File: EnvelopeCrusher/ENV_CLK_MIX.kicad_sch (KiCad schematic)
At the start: 15 parts, among them U6 TL072

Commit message: Completed Schematic
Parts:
- gave numbers to parts that had none: 13
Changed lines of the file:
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@@
   (symbol (lib_id "Device:R") (at 119.38 86.36 90) (mirror x) (unit 1)
     (in_bom yes) (on_board yes)
-    (property "Reference" "R?" (id 0) (at 119.38 83.82 90))
+    (property "Reference" "R26" (id 0) (at 119.38 83.82 90))
     (property "Value" "10K" (id 1) (at 119.38 88.9 90))
     (property "Footprint" "Resistor_SMD:R_0805_2012Metric_Pad1.20x1.40mm_HandSolder" (id 2) (at 119.38 84.582 90)
@@
   (symbol (lib_id "power:+5V") (at 44.45 133.9779 0) (unit 1)
     (in_bom yes) (on_board yes) (fields_autoplaced)
-    (property "Reference" "#PWR?" (id 0) (at 44.45 137.7879 0)
+    (property "Reference" "#PWR069" (id 0) (at 44.45 137.7879 0)
       (effects (font (size 1.27 1.27)) hide)
     )
@@
   (symbol (lib_id "Jumper:SolderJumper_2_Bridged") (at 101.6 58.42 0) (unit 1)
     (in_bom yes) (on_board yes)
-    (property "Reference" "JP?" (id 0) (at 101.6 55.88 0))
+    (property "Reference" "JP8" (id 0) (at 101.6 55.88 0))
     (property "Value" "SolderJumper_2_Bridged" (id 1) (at 101.6 54.61 0)
       (effects (font (size 1.27 1.27)) hide)
@@
   (symbol (lib_id "power:GND") (at 138.43 106.68 0) (unit 1)
     (in_bom yes) (on_board yes) (fields_autoplaced)
-    (property "Reference" "#PWR?" (id 0) (at 138.43 113.03 0)
+    (property "Reference" "#PWR073" (id 0) (at 138.43 113.03 0)
       (effects (font (size 1.27 1.27)) hide)
     )
@@
   (symbol (lib_id "Device:R") (at 119.38 95.25 90) (mirror x) (unit 1)
     (in_bom yes) (on_board yes)
-    (property "Reference" "R?" (id 0) (at 119.38 92.71 90))
+    (property "Reference" "R27" (id 0) (at 119.38 92.71 90))
     (property "Value" "10K" (id 1) (at 119.38 97.79 90))
     (property "Footprint" "Resistor_SMD:R_0805_2012Metric_Pad1.20x1.40mm_HandSolder" (id 2) (at 119.38 93.472 90)
@@
   (symbol (lib_id "Jumper:SolderJumper_2_Bridged") (at 101.6 95.25 0) (unit 1)
     (in_bom yes) (on_board yes)
-    (property "Reference" "JP?" (id 0) (at 101.6 92.71 0))
+    (property "Reference" "JP10" (id 0) (at 101.6 92.71 0))
     (property "Value" "SolderJumper_2_Bridged" (id 1) (at 101.6 91.44 0)
       (effects (font (size 1.27 1.27)) hide)
@@
   (symbol (lib_id "Device:C") (at 120.65 149.86 180) (unit 1)
     (in_bom yes) (on_board yes)
-    (property "Reference" "C?" (id 0) (at 121.92 147.32 0)
+    (property "Reference" "C50" (id 0) (at 121.92 147.32 0)
       (effects (font (size 1.27 1.27)) (justify right))
     )
@@
   (symbol (lib_id "power:GND") (at 31.75 160.02 0) (unit 1)
     (in_bom yes) (on_board yes) (fields_autoplaced)
-    (property "Reference" "#PWR?" (id 0) (at 31.75 166.37 0)
+    (property "Reference" "#PWR068" (id 0) (at 31.75 166.37 0)
       (effects (font (size 1.27 1.27)) hide)
     )
@@
   (symbol (lib_id "power:-5V") (at 107.95 133.9779 0) (unit 1)
     (in_bom yes) (on_board yes) (fields_autoplaced)
-    (property "Reference" "#PWR?" (id 0) (at 107.95 131.4379 0)
+    (property "Reference" "#PWR070" (id 0) (at 107.95 131.4379 0)
       (effects (font (size 1.27 1.27)) hide)
     )
@@
   (symbol (lib_id "Jumper:SolderJumper_2_Bridged") (at 101.6 86.36 0) (unit 1)
     (in_bom yes) (on_board yes)
-    (property "Reference" "JP?" (id 0) (at 101.6 83.82 0))
+    (property "Reference" "JP9" (id 0) (at 101.6 83.82 0))
     (property "Value" "SolderJumper_2_Bridged" (id 1) (at 101.6 82.55 0)
       (effects (font (size 1.27 1.27)) hide)
@@
   (symbol (lib_id "Device:R") (at 119.38 49.53 90) (mirror x) (unit 1)
     (in_bom yes) (on_board yes)
-    (property "Reference" "R?" (id 0) (at 119.38 46.99 90))
+    (property "Reference" "R24" (id 0) (at 119.38 46.99 90))
     (property "Value" "10K" (id 1) (at 119.38 52.07 90))
     (property "Footprint" "Resistor_SMD:R_0805_2012Metric_Pad1.20x1.40mm_HandSolder" (id 2) (at 119.38 47.752 90)
@@
   (symbol (lib_id "Device:R") (at 119.38 58.42 90) (mirror x) (unit 1)
     (in_bom yes) (on_board yes)
-    (property "Reference" "R?" (id 0) (at 119.38 55.88 90))
+    (property "Reference" "R25" (id 0) (at 119.38 55.88 90))
     (property "Value" "10K" (id 1) (at 119.38 60.96 90))
     (property "Footprint" "Resistor_SMD:R_0805_2012Metric_Pad1.20x1.40mm_HandSolder" (id 2) (at 119.38 56.642 90)
@@
   (symbol (lib_id "Amplifier_Operational:TL072") (at 148.59 97.79 0) (mirror x) (unit 1)
     (in_bom yes) (on_board yes)
-    (property "Reference" "U?" (id 0) (at 148.59 104.14 0))
+    (property "Reference" "U14" (id 0) (at 148.59 104.14 0))
     (property "Value" "TL072" (id 1) (at 148.59 106.68 0))
     (property "Footprint" "" (id 2) (at 148.59 97.79 0)
@@
   (symbol (lib_id "Jumper:SolderJumper_2_Bridged") (at 101.6 49.53 0) (unit 1)
     (in_bom yes) (on_board yes)
-    (property "Reference" "JP?" (id 0) (at 101.6 46.99 0))
+    (property "Reference" "JP7" (id 0) (at 101.6 46.99 0))
     (property "Value" "SolderJumper_2_Bridged" (id 1) (at 101.6 45.72 0)
       (effects (font (size 1.27 1.27)) hide)
@@
   (symbol (lib_id "power:GND") (at 138.43 69.85 0) (unit 1)
     (in_bom yes) (on_board yes) (fields_autoplaced)
-    (property "Reference" "#PWR?" (id 0) (at 138.43 76.2 0)
+    (property "Reference" "#PWR072" (id 0) (at 138.43 76.2 0)
       (effects (font (size 1.27 1.27)) hide)
     )
@@
   (symbol (lib_id "Device:C") (at 31.75 149.86 180) (unit 1)
     (in_bom yes) (on_board yes)
-    (property "Reference" "C?" (id 0) (at 33.02 147.32 0)
+    (property "Reference" "C48" (id 0) (at 33.02 147.32 0)
       (effects (font (size 1.27 1.27)) (justify right))
     )
@@
   (symbol (lib_id "Device:C") (at 76.2 149.86 90) (unit 1)
     (in_bom yes) (on_board yes)
-    (property "Reference" "C?" (id 0) (at 76.2 146.05 90))
+    (property "Reference" "C49" (id 0) (at 76.2 146.05 90))
     (property "Value" "100nF" (id 1) (at 76.2 153.67 90))
     (property "Footprint" "Capacitor_SMD:C_0805_2012Metric_Pad1.18x1.45mm_HandSolder" (id 2) (at 80.01 148.8948 0)
@@
   (symbol (lib_id "Device:R") (at 148.59 49.53 90) (mirror x) (unit 1)
     (in_bom yes) (on_board yes)
-    (property "Reference" "R?" (id 0) (at 148.59 46.99 90))
+    (property "Reference" "R28" (id 0) (at 148.59 46.99 90))
     (property "Value" "10K" (id 1) (at 148.59 52.07 90))
     (property "Footprint" "Resistor_SMD:R_0805_2012Metric_Pad1.20x1.40mm_HandSolder" (id 2) (at 148.59 47.752 90)
@@
   (symbol (lib_id "power:GND") (at 120.65 160.02 0) (unit 1)
     (in_bom yes) (on_board yes) (fields_autoplaced)
-    (property "Reference" "#PWR?" (id 0) (at 120.65 166.37 0)
-      (effects (font (size 1.27 1.27)) hide)
-    )
+    (property "Reference" "#PWR071" (id 0) (at 120.65 166.37 0)
+      (effects (font (size 1.27 1.27)) hide)
+    )

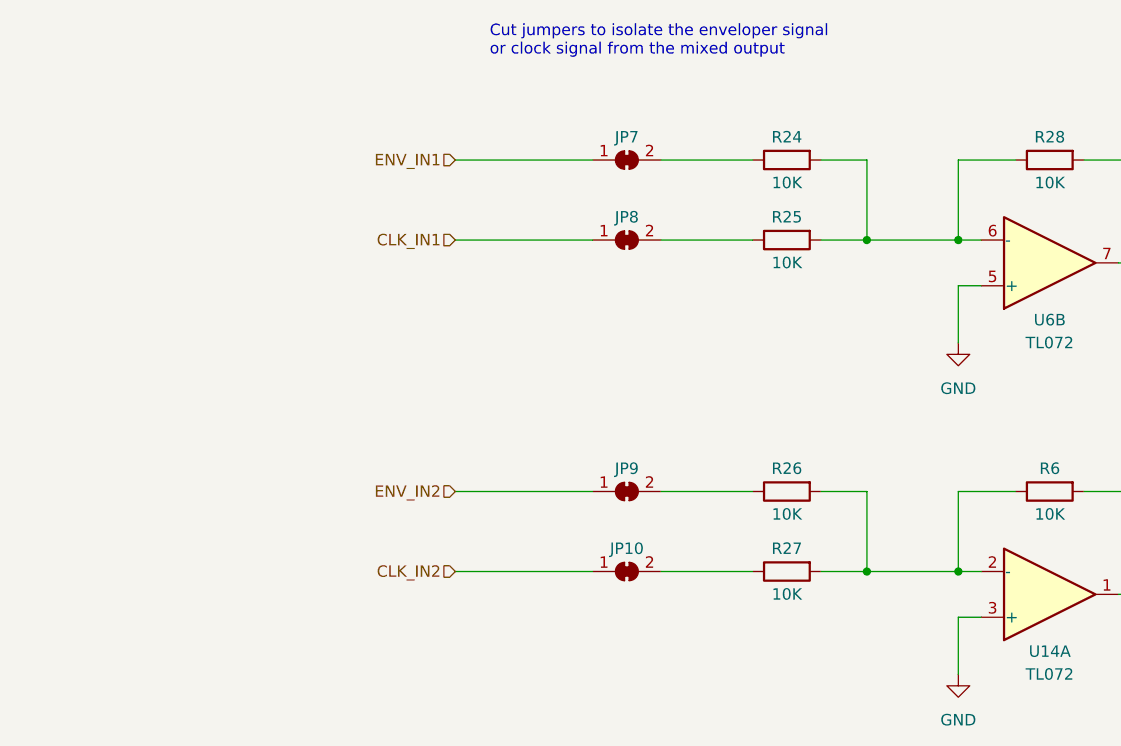
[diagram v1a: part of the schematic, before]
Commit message: Updated schematic
- Replaced CD4066 (SOIC14) with DG611 (QFN16)
- Replaced CLK/ENV mixer jumpers with 4xSPST DIPSW
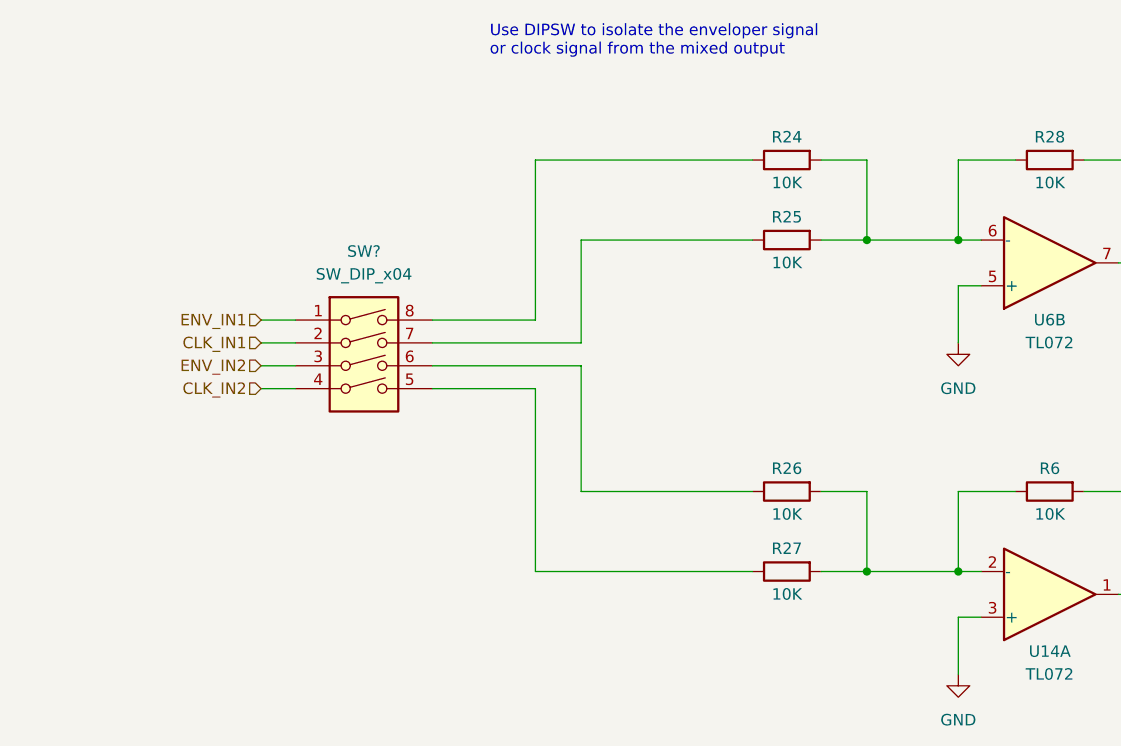
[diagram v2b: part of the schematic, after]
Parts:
- removed JP10, JP7, JP8, JP9: SolderJumper_2_Bridged, Jumper:SolderJumper-2_P1.3mm_Bridged_Pad1.0x1.5mm, symbol Jumper:SolderJumper_2_Bridged
- added SW?: SW_DIP_x04, symbol Switch:SW_DIP_x04
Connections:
- net CLK_IN1: now also SW?.2
- net CLK_IN2: now also SW?.4
- net ENV_IN1: now also SW?.1
- net ENV_IN2: now also SW?.3
- net at R26.1: now also SW?.6
- net at R25.1: now also SW?.7
- net at R27.1: now also SW?.5
- net at R24.1: now also SW?.8
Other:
- note added: "Use DIPSW to isolate the enveloper signal or clock signal from the mixed output"
- note removed: "Cut jumpers to isolate the enveloper signal or clock signal from the mixed output"
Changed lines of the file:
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@@
   (junction (at 44.45 139.7) (diameter 0) (color 0 0 0 0)
   )
+  (wire (pts (xy 80.01 67.31) (xy 91.44 67.31))
+    (stroke (width 0) (type default) (color 0 0 0 0))
+  )
   (wire (pts (xy 160.02 60.96) (xy 156.21 60.96))
     (stroke (width 0) (type default) (color 0 0 0 0))
@@
     (stroke (width 0) (type default) (color 0 0 0 0))
   )
+  (wire (pts (xy 60.96 74.93) (xy 64.77 74.93))
+    (stroke (width 0) (type default) (color 0 0 0 0))
+  )
   (wire (pts (xy 128.27 95.25) (xy 138.43 95.25))
     (stroke (width 0) (type default) (color 0 0 0 0))
@@
     (stroke (width 0) (type default) (color 0 0 0 0))
   )
-  (wire (pts (xy 105.41 86.36) (xy 115.57 86.36))
+  (wire (pts (xy 96.52 86.36) (xy 115.57 86.36))
     (stroke (width 0) (type default) (color 0 0 0 0))
   )
@@
     (stroke (width 0) (type default) (color 0 0 0 0))
   )
-  (wire (pts (xy 105.41 95.25) (xy 115.57 95.25))
+  (wire (pts (xy 91.44 95.25) (xy 115.57 95.25))
     (stroke (width 0) (type default) (color 0 0 0 0))
   )
@@
     (stroke (width 0) (type default) (color 0 0 0 0))
   )
+  (wire (pts (xy 60.96 67.31) (xy 64.77 67.31))
+    (stroke (width 0) (type default) (color 0 0 0 0))
+  )
+  (wire (pts (xy 60.96 72.39) (xy 64.77 72.39))
+    (stroke (width 0) (type default) (color 0 0 0 0))
+  )
   (wire (pts (xy 63.5 139.7) (xy 68.58 139.7))
     (stroke (width 0) (type default) (color 0 0 0 0))
@@
     (stroke (width 0) (type default) (color 0 0 0 0))
   )
-  (wire (pts (xy 82.55 49.53) (xy 97.79 49.53))
-    (stroke (width 0) (type default) (color 0 0 0 0))
-  )
-  (wire (pts (xy 105.41 49.53) (xy 115.57 49.53))
+  (wire (pts (xy 91.44 49.53) (xy 115.57 49.53))
     (stroke (width 0) (type default) (color 0 0 0 0))
   )
@@
     (stroke (width 0) (type default) (color 0 0 0 0))
   )
+  (wire (pts (xy 96.52 69.85) (xy 80.01 69.85))
+    (stroke (width 0) (type default) (color 0 0 0 0))
+  )
   (wire (pts (xy 80.01 149.86) (xy 90.17 149.86))
     (stroke (width 0) (type default) (color 0 0 0 0))
@@
     (stroke (width 0) (type default) (color 0 0 0 0))
   )
+  (wire (pts (xy 91.44 74.93) (xy 80.01 74.93))
+    (stroke (width 0) (type default) (color 0 0 0 0))
+  )
   (wire (pts (xy 140.97 100.33) (xy 138.43 100.33))
     (stroke (width 0) (type default) (color 0 0 0 0))
@@
     (stroke (width 0) (type default) (color 0 0 0 0))
   )
+  (wire (pts (xy 96.52 72.39) (xy 96.52 86.36))
+    (stroke (width 0) (type default) (color 0 0 0 0))
+  )
   (wire (pts (xy 44.45 139.7) (xy 44.45 176.53))
     (stroke (width 0) (type default) (color 0 0 0 0))
@@
     (stroke (width 0) (type default) (color 0 0 0 0))
   )
-  (wire (pts (xy 82.55 95.25) (xy 97.79 95.25))
-    (stroke (width 0) (type default) (color 0 0 0 0))
-  )
   (wire (pts (xy 152.4 86.36) (xy 160.02 86.36))
     (stroke (width 0) (type default) (color 0 0 0 0))
@@
     (stroke (width 0) (type default) (color 0 0 0 0))
   )
+  (wire (pts (xy 80.01 72.39) (xy 96.52 72.39))
+    (stroke (width 0) (type default) (color 0 0 0 0))
+  )
+  (wire (pts (xy 60.96 69.85) (xy 64.77 69.85))
+    (stroke (width 0) (type default) (color 0 0 0 0))
+  )
   (wire (pts (xy 160.02 97.79) (xy 167.64 97.79))
     (stroke (width 0) (type default) (color 0 0 0 0))
@@
     (stroke (width 0) (type default) (color 0 0 0 0))
   )
-  (wire (pts (xy 82.55 58.42) (xy 97.79 58.42))
-    (stroke (width 0) (type default) (color 0 0 0 0))
-  )
   (wire (pts (xy 138.43 63.5) (xy 138.43 69.85))
     (stroke (width 0) (type default) (color 0 0 0 0))
   )
-  (wire (pts (xy 82.55 86.36) (xy 97.79 86.36))
+  (wire (pts (xy 91.44 95.25) (xy 91.44 74.93))
+    (stroke (width 0) (type default) (color 0 0 0 0))
+  )
+  (wire (pts (xy 91.44 67.31) (xy 91.44 49.53))
     (stroke (width 0) (type default) (color 0 0 0 0))
   )
@@
     (stroke (width 0) (type default) (color 0 0 0 0))
   )
-  (wire (pts (xy 105.41 58.42) (xy 115.57 58.42))
+  (wire (pts (xy 96.52 58.42) (xy 115.57 58.42))
     (stroke (width 0) (type default) (color 0 0 0 0))
   )
@@
     (stroke (width 0) (type default) (color 0 0 0 0))
   )
+  (wire (pts (xy 96.52 58.42) (xy 96.52 69.85))
+    (stroke (width 0) (type default) (color 0 0 0 0))
+  )
   (wire (pts (xy 123.19 58.42) (xy 128.27 58.42))
     (stroke (width 0) (type default) (color 0 0 0 0))
@@
     (stroke (width 0) (type default) (color 0 0 0 0))
   )
-  (text "Cut jumpers to isolate the enveloper signal \nor clock signal from the mixed output"
+  (text "Use DIPSW to isolate the enveloper signal \nor clock signal from the mixed output"
     (at 86.36 38.1 0)
     (effects (font (size 1.27 1.27)) (justify left bottom))
   )
-  (hierarchical_label "ENV_IN2" (shape input) (at 82.55 86.36 180)
+  (hierarchical_label "ENV_IN2" (shape input) (at 60.96 72.39 180)
     (effects (font (size 1.27 1.27)) (justify right))
   )
@@
     (effects (font (size 1.27 1.27)) (justify left))
   )
-  (hierarchical_label "CLK_IN2" (shape input) (at 82.55 95.25 180)
+  (hierarchical_label "CLK_IN2" (shape input) (at 60.96 74.93 180)
     (effects (font (size 1.27 1.27)) (justify right))
   )
-  (hierarchical_label "CLK_IN1" (shape input) (at 82.55 58.42 180)
+  (hierarchical_label "CLK_IN1" (shape input) (at 60.96 69.85 180)
     (effects (font (size 1.27 1.27)) (justify right))
   )
-  (hierarchical_label "ENV_IN1" (shape input) (at 82.55 49.53 180)
+  (hierarchical_label "ENV_IN1" (shape input) (at 60.96 67.31 180)
     (effects (font (size 1.27 1.27)) (justify right))
   )
@@
     (pin "1")
   )
-  (symbol (lib_id "Jumper:SolderJumper_2_Bridged") (at 101.6 58.42 0) (unit 1)
-    (in_bom yes) (on_board yes)
-    (property "Reference" "JP8" (id 0) (at 101.6 55.88 0))
-    (property "Value" "SolderJumper_2_Bridged" (id 1) (at 101.6 54.61 0)
-      (effects (font (size 1.27 1.27)) hide)
-    )
-    (property "Footprint" "Jumper:SolderJumper-2_P1.3mm_Bridged_Pad1.0x1.5mm" (id 2) (at 101.6 58.42 0)
-      (effects (font (size 1.27 1.27)) hide)
-    )
-    (property "Datasheet" "~" (id 3) (at 101.6 58.42 0)
-      (effects (font (size 1.27 1.27)) hide)
-    )
-    (pin "1")
-    (pin "2")
-  )
   (symbol (lib_id "power:GND") (at 138.43 106.68 0) (unit 1)
     (in_bom yes) (on_board yes) (fields_autoplaced)
@@
     (pin "2")
   )
-  (symbol (lib_id "Jumper:SolderJumper_2_Bridged") (at 101.6 95.25 0) (unit 1)
-    (in_bom yes) (on_board yes)
-    (property "Reference" "JP10" (id 0) (at 101.6 92.71 0))
-    (property "Value" "SolderJumper_2_Bridged" (id 1) (at 101.6 91.44 0)
-      (effects (font (size 1.27 1.27)) hide)
-    )
-    (property "Footprint" "Jumper:SolderJumper-2_P1.3mm_Bridged_Pad1.0x1.5mm" (id 2) (at 101.6 95.25 0)
-      (effects (font (size 1.27 1.27)) hide)
-    )
-    (property "Datasheet" "~" (id 3) (at 101.6 95.25 0)
-      (effects (font (size 1.27 1.27)) hide)
-    )
-    (pin "1")
-    (pin "2")
+  (symbol (lib_id "Switch:SW_DIP_x04") (at 72.39 72.39 0) (unit 1)
+    (in_bom yes) (on_board yes) (fields_autoplaced)
+    (property "Reference" "SW?" (id 0) (at 72.39 59.69 0))
+    (property "Value" "SW_DIP_x04" (id 1) (at 72.39 62.23 0))
+    (property "Footprint" "" (id 2) (at 72.39 72.39 0)
+      (effects (font (size 1.27 1.27)) hide)
+    )
+    (property "Datasheet" "~" (id 3) (at 72.39 72.39 0)
+      (effects (font (size 1.27 1.27)) hide)
+    )
+    (pin "1")
+    (pin "2")
+    (pin "3")
+    (pin "4")
+    (pin "5")
+    (pin "6")
+    (pin "7")
+    (pin "8")
   )
   (symbol (lib_id "Device:C") (at 120.65 149.86 180) (unit 1)
@@
     )
     (pin "1")
-  )
-  (symbol (lib_id "Jumper:SolderJumper_2_Bridged") (at 101.6 86.36 0) (unit 1)
-    (in_bom yes) (on_board yes)
-    (property "Reference" "JP9" (id 0) (at 101.6 83.82 0))
-    (property "Value" "SolderJumper_2_Bridged" (id 1) (at 101.6 82.55 0)
-      (effects (font (size 1.27 1.27)) hide)
-    )
-    (property "Footprint" "Jumper:SolderJumper-2_P1.3mm_Bridged_Pad1.0x1.5mm" (id 2) (at 101.6 86.36 0)
-      (effects (font (size 1.27 1.27)) hide)
-    )
-    (property "Datasheet" "~" (id 3) (at 101.6 86.36 0)
-      (effects (font (size 1.27 1.27)) hide)
-    )
-    (pin "1")
-    (pin "2")
   )
   (symbol (lib_id "Device:R") (at 119.38 49.53 90) (mirror x) (unit 1)
@@
     (pin "8")
   )
-  (symbol (lib_id "Jumper:SolderJumper_2_Bridged") (at 101.6 49.53 0) (unit 1)
-    (in_bom yes) (on_board yes)
-    (property "Reference" "JP7" (id 0) (at 101.6 46.99 0))
-    (property "Value" "SolderJumper_2_Bridged" (id 1) (at 101.6 45.72 0)
-      (effects (font (size 1.27 1.27)) hide)
-    )
-    (property "Footprint" "Jumper:SolderJumper-2_P1.3mm_Bridged_Pad1.0x1.5mm" (id 2) (at 101.6 49.53 0)
-      (effects (font (size 1.27 1.27)) hide)
-    )
-    (property "Datasheet" "~" (id 3) (at 101.6 49.53 0)
-      (effects (font (size 1.27 1.27)) hide)
-    )
-    (pin "1")
-    (pin "2")
-  )
   (symbol (lib_id "power:GND") (at 138.43 69.85 0) (unit 1)
